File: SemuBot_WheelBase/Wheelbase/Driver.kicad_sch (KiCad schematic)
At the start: 23 parts, among them IC1 DRV8353FSRTAR, Q1 AON7262E, Q19 AON7262E, Q2 AON7262E, Q3 AON7262E, Q5 AON7262E, Q6 AON7262E

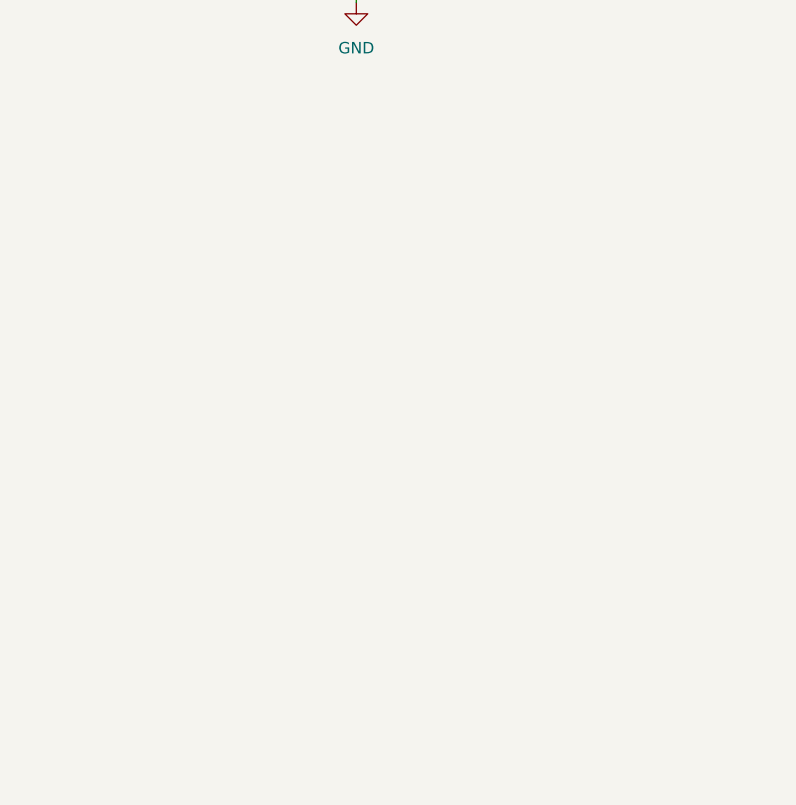
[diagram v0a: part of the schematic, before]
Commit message: Wheelbase development and repo cleanup
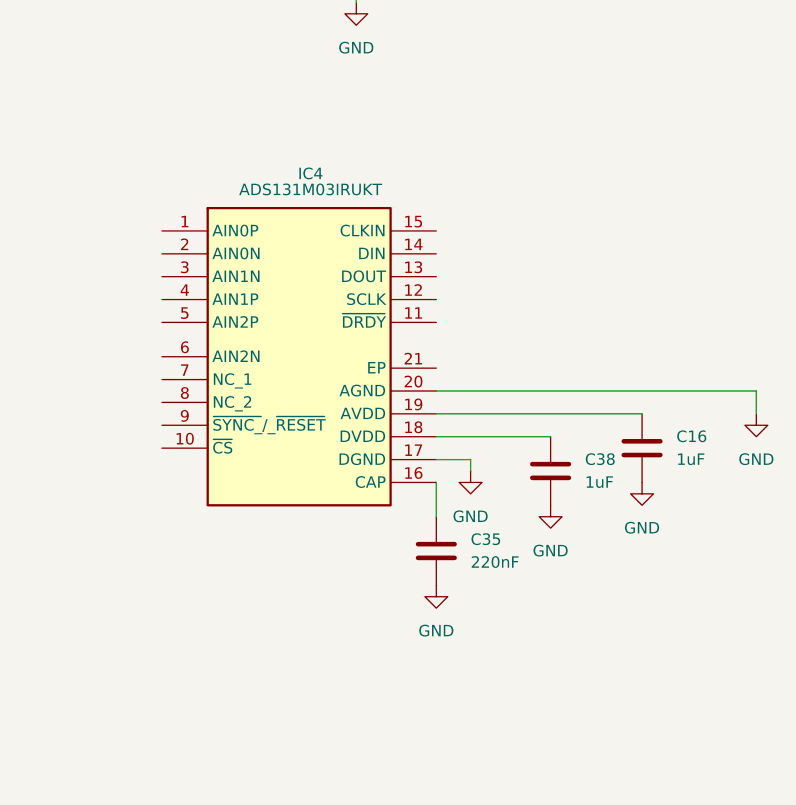
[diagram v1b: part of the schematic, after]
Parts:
- added C16, C38: 1uF, Capacitor_SMD:C_0603_1608Metric_Pad1.08x0.95mm_HandSolder, symbol Device:C
- added C35: 220nF, Capacitor_SMD:C_0603_1608Metric_Pad1.08x0.95mm_HandSolder, symbol Device:C
- added IC4: ADS131M03IRUKT, QFN40P300X300X80-21N-D, symbol ADS131M03IRUKT:ADS131M03IRUKT
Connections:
- net GND: now also C16.1, C35.1, C38.1, IC4.17 (DGND), IC4.20 (AGND)
- new net: C35.2, IC4.16 (CAP)
- new net: C38.2, IC4.18 (DVDD)
- new net: C16.2, IC4.19 (AVDD)

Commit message: Current sensing
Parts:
- removed D4: LED, LED_SMD:LED_0603_1608Metric_Pad1.05x0.95mm_HandSolder, symbol Device:LED
- removed R3: 3.3K, Resistor_SMD:R_0603_1608Metric_Pad0.98x0.95mm_HandSolder, symbol Device:R
- added C51: 100nF, Capacitor_SMD:C_0603_1608Metric_Pad1.08x0.95mm_HandSolder, symbol Device:C
- added R32: 1.5K, Resistor_SMD:R_0603_1608Metric_Pad0.98x0.95mm_HandSolder, symbol Device:R
- C16: value 1uF -> 220nF
- C35: value 220nF -> 100nF
- C38: value 1uF -> 100nF
- renumbered R32 to R3
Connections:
- net +5V: now also R32.2; no longer C6.1, IC1.24 (VREF), R3.2, R4.2
- net GND: now also C35.2, C38.2, IC4.19 (AVDD), IC4.2 (AIN0N), IC4.21 (EP), IC4.3 (AIN1N), IC4.6 (AIN2N), C51.2; no longer C35.1, C38.1
- net HAL_2: now also R32.1; no longer R3.1
- net SCLK: now also IC4.12 (SCLK)
- net SDI: now also IC4.13 (DOUT)
- net SDO: now also IC4.14 (DIN)
- net SOC: now reaches IC1.21 (SOC)
- net SOC: now also IC4.5 (AIN2P)
- net SOB: now reaches IC1.22 (SOB)
- net SOB: now also IC4.4 (AIN1P)
- net SOA: now reaches IC1.23 (SOA)
- net SOA: now also IC4.1 (AIN0P)
- net at IC1.26 (NFAULT): now also R4.1
- net at IC4.16 (CAP): now also C16.2; no longer C35.2
- net ADC_CS: now reaches IC4.10 (~{CS})
- net DRDY: now reaches IC4.11 (~{DRDY})
- net adc_CLK: now reaches IC4.15 (CLKIN)
- net +3.3V: now reaches IC4.18 (DVDD)
- net +3.3V: now also C35.1, C38.1, C6.1, IC1.24 (VREF), R3.2, R4.2, C51.1; no longer C38.2
- net at IC4.9 (~{SYNC_}/_~{RESET}): now also R3.1
- no-connect marks 3 -> 2
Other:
- moved on the sheet: C31, C5, C6, IC4, R3
